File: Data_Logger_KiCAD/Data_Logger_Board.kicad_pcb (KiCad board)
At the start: 6 copper layers, 45 x 63 mm, 107 parts, among them J1 USB_C_Receptacle_USB2.0_16P, J2 Screw_Terminal_01x02, J3 Micro_SD_Card, J4 Conn_Coaxial_Small, J5 Conn_01x02, Q1 Q_NMOS_GSD, SW1 SW_Push, SW2 SW_Push, U1 LSM6DSO32TR, U10 BMP390L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

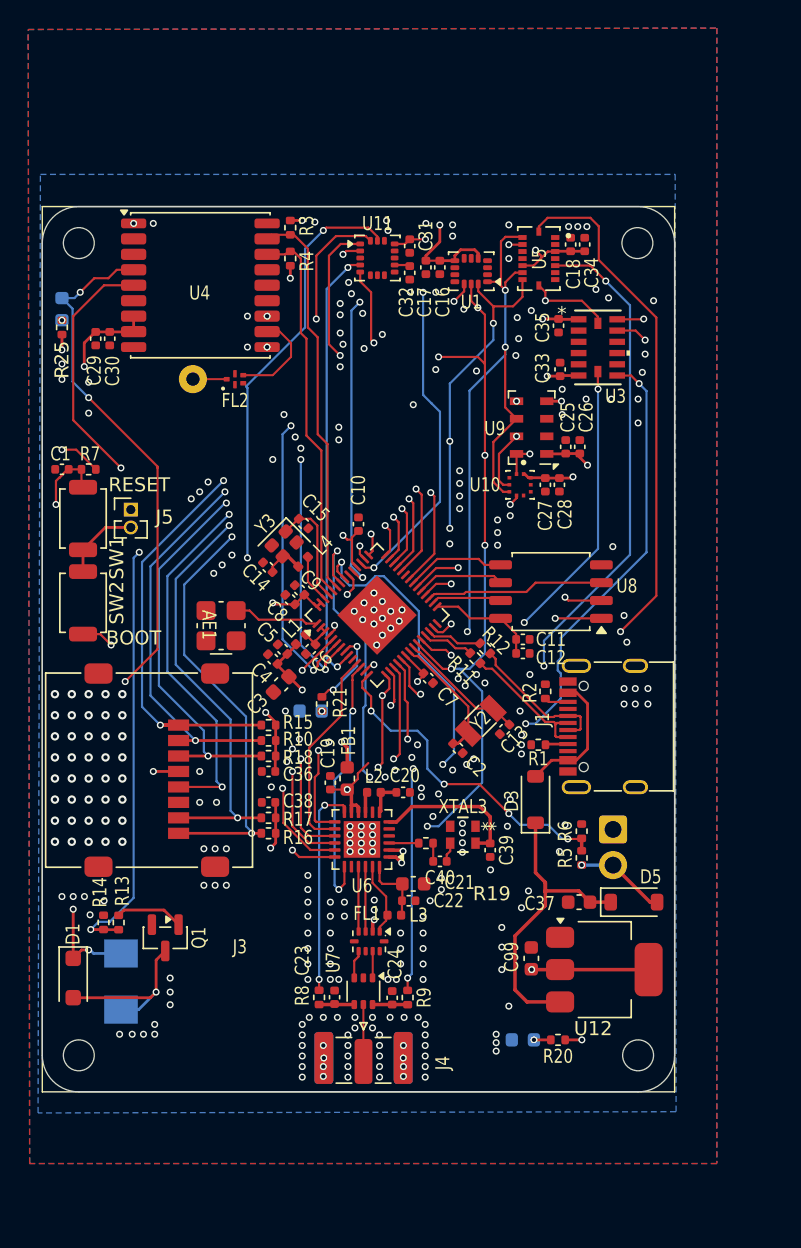
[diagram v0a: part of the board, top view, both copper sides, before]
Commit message: add stitching vias
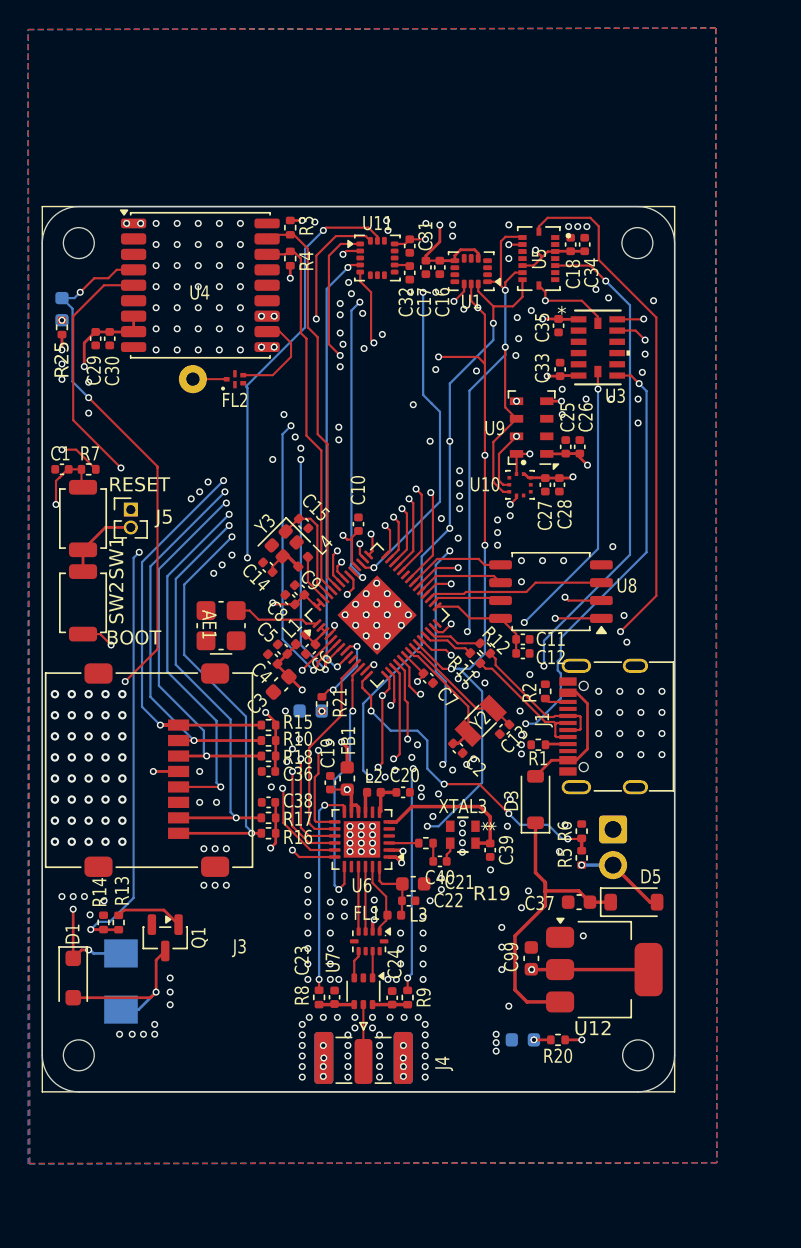
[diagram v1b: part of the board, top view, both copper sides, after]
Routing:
- net /MCU/ANT_SW: track 40.1 -> 43.7 mm, vias 4 -> 5
- net /MCU/MOSI: track 109.8 -> 112.7 mm
- net Net-(U6-VBAT): track 15.5 -> 13.0 mm
- net GND: vias 288 -> 342

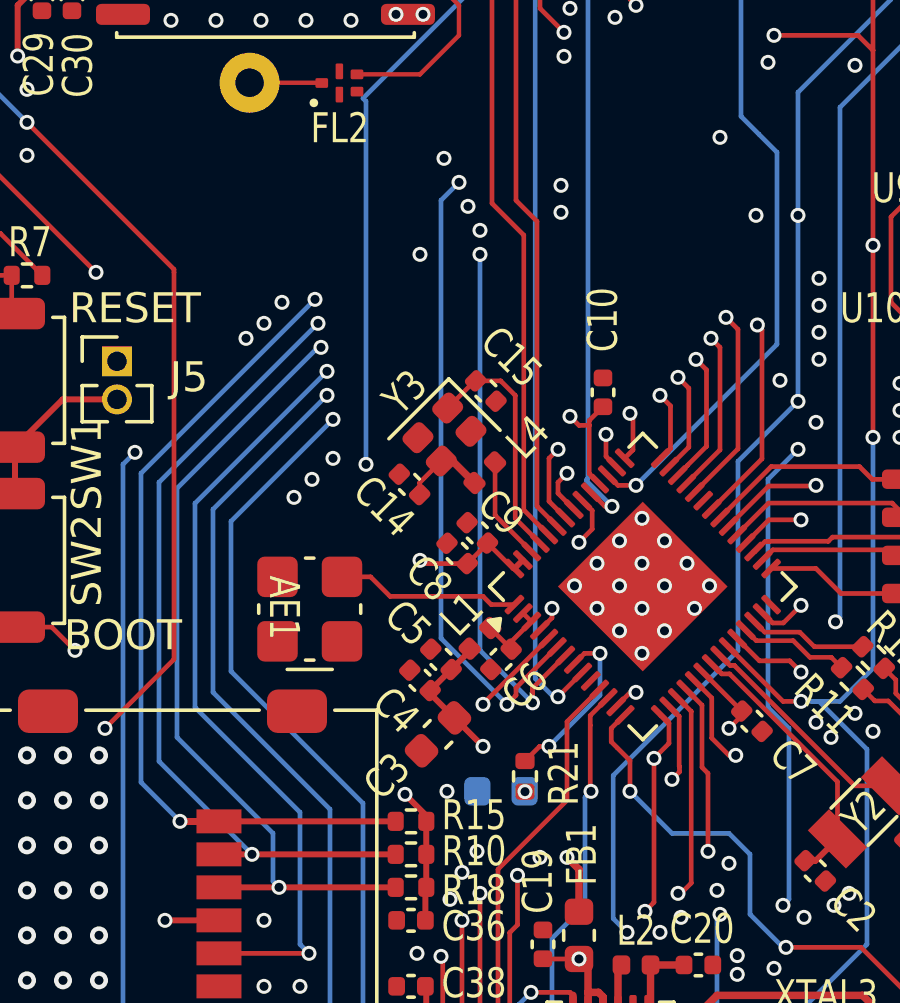
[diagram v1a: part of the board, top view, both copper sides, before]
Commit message: fix missing gnd
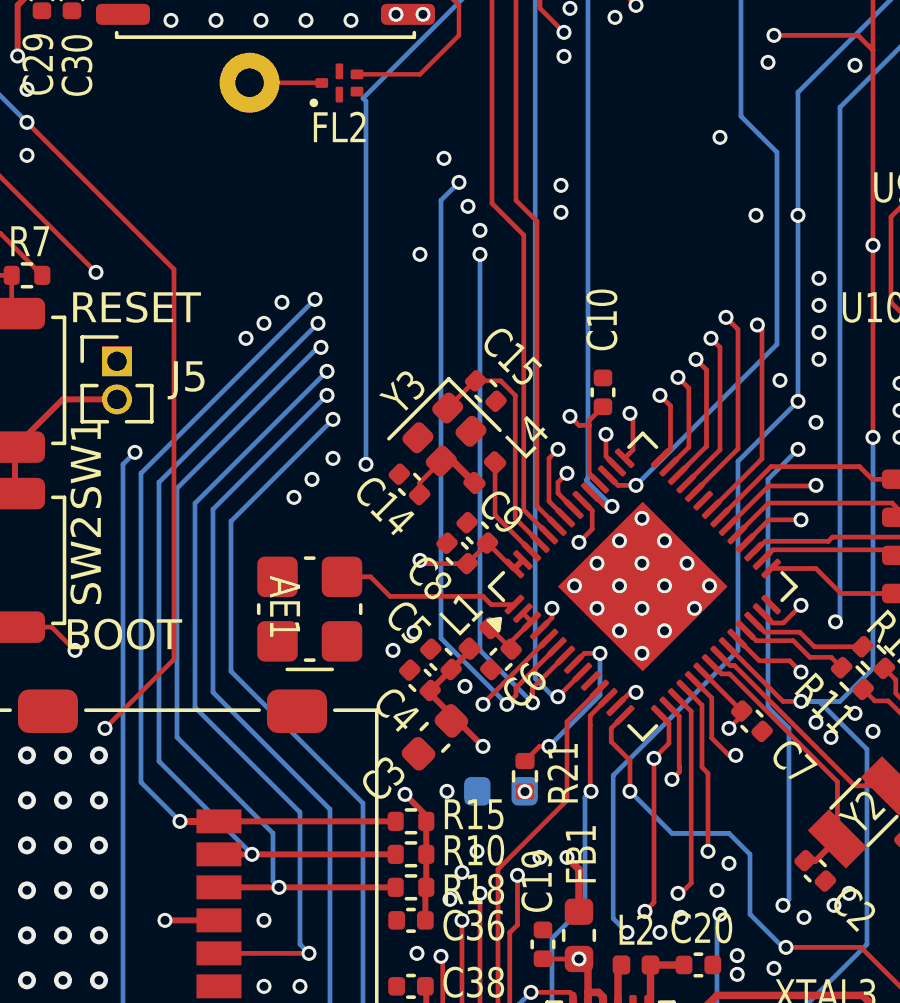
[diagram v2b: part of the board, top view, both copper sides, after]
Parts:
- moved C3 0.14 mm to (136.9, 81.2)
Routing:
- net GND: vias 342 -> 345
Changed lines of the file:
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@@
 	(footprint "Capacitor_SMD:C_0603_1608Metric"
 		(layer "F.Cu")
-		(at 137 81.1 -135)
+		(at 136.9 81.2 -135)
 		(descr "Capacitor SMD 0603 (1608 Metric), square (rectangular) end terminal, IPC-7351 nominal, (Body size source: IPC-SM-782 page 76, https://www.pcb-3d.com/wordpress/wp-content/uploads/ipc-sm-782a_amendment_1_and_2.pdf), generated with kicad-footprint-generator")
 		(tags "capacitor")
@@
 	)
 	(via
+		(at 137.9 79.5)
+		(size 0.5)
+		(drill 0.3)
+		(layers "F.Cu" "B.Cu")
+		(free yes)
+		(net 1)
+	)
+	(via
 		(at 141.75 107.55)
 		(size 0.5)
@@
 	)
 	(via
+		(at 136.2 77.7)
+		(size 0.5)
+		(drill 0.3)
+		(layers "F.Cu" "B.Cu")
+		(free yes)
+		(net 1)
+	)
+	(via
 		(at 138.5 107.55)
 		(size 0.5)
@@
 	)
 	(via
+		(at 135.5 78.3)
+		(size 0.5)
+		(drill 0.3)
+		(layers "F.Cu" "B.Cu")
+		(free yes)
+		(net 1)
+	)
+	(via
 		(at 164.1 84.6)
 		(size 0.5)
@@
 	)
 	(segment
-		(start 121.6 70.9)
-		(end 130.2 79.5)
+		(start 120.975 68.3)
+		(end 121.6 68.925)
 		(width 0.1565)
 		(layer "In2.Cu")
@@
 	)
 	(segment
-		(start 130.2 79.5)
-		(end 138.2 79.5)
+		(start 136.9 79.5)
+		(end 139.5 76.9)
 		(width 0.1565)
 		(layer "In2.Cu")
@@
 	)
 	(segment
-		(start 138.2 79.5)
-		(end 140.8 76.9)
+		(start 121.6 68.925)
+		(end 121.6 70.9)
 		(width 0.1565)
 		(layer "In2.Cu")
@@
 	)
 	(segment
-		(start 121.6 68.925)
-		(end 121.6 70.9)
+		(start 121.6 70.9)
+		(end 130.2 79.5)
 		(width 0.1565)
 		(layer "In2.Cu")
@@
 	)
 	(segment
-		(start 120.975 68.3)
-		(end 121.6 68.925)
+		(start 130.2 79.5)
+		(end 136.9 79.5)
+		(width 0.1565)
+		(layer "In2.Cu")
+		(net 3)
+	)
+	(segment
+		(start 139.5 76.9)
+		(end 140.8 76.9)
 		(width 0.1565)
 		(layer "In2.Cu")
@@
 	)
 	(segment
-		(start 155.9 60.95)
-		(end 156.95 60.95)
-		(width 0.2)
+		(start 139.3 80.1)
+		(end 139.6 79.8)
+		(width 0.1565)
 		(layer "F.Cu")
 		(net 62)
 	)
 	(segment
-		(start 139.6 79.8)
-		(end 139.3 80.1)
-		(width 0.1565)
+		(start 155.9 60.95)
+		(end 156.95 60.95)
+		(width 0.2)
 		(layer "F.Cu")
 		(net 62)
 	)
 	(segment
-		(start 140.961218 78.188349)
-		(end 139.6 79.549567)
+		(start 139.6 79.549567)
+		(end 140.961218 78.188349)
 		(width 0.1565)
 		(layer "F.Cu")
@@
 	)
 	(segment
-		(start 139.6 79.549567)
-		(end 139.6 79.8)
+		(start 139.6 79.8)
+		(end 139.6 79.549567)
 		(width 0.1565)
 		(layer "F.Cu")
@@
 	(segment
 		(start 137.1 77.9)
-		(end 139.3 80.1)
+		(end 137.1 63.3)
 		(width 0.1565)
 		(layer "B.Cu")
@@
 	)
 	(segment
-		(start 137.7 62.7)
-		(end 137.1 63.3)
+		(start 137.1 63.3)
+		(end 137.7 62.7)
 		(width 0.1565)
 		(layer "B.Cu")
@@
 	)
 	(segment
-		(start 137.1 63.3)
+		(start 139.3 80.1)
 		(end 137.1 77.9)
 		(width 0.1565)
@@
 	)
 	(zone
-		(net 77)
-		(net_name "Net-(AE2-A)")
+		(net 82)
+		(net_name "/MCU/SMA_CONN")
 		(layer "F.Cu")
 		(name "$teardrop_padvia$")
 		(hatch none 0.1)
-		(priority 30000)
+		(priority 30001)
 		(attr
 			(teardrop
@@
 		(polygon
 			(pts
-				(xy 132.700785 59.45415) (xy 132.700785 59.30585) (xy 131.27557 58.54853) (xy 130.719 59.38) (xy 131.27557 60.21147)
+				(xy 142.92415 105.7025) (xy 142.77585 105.7025) (xy 142.298223 106.410723) (xy 142.86 107.9385)
+				(xy 143.421777 106.410723)
 			)
 		)
 	)
 	(zone
-		(net 82)
-		(net_name "/MCU/SMA_CONN")
+		(net 77)
+		(net_name "Net-(AE2-A)")
 		(layer "F.Cu")
 		(name "$teardrop_padvia$")
 		(hatch none 0.1)
-		(priority 30001)
+		(priority 30000)
 		(attr
 			(teardrop
@@
 		(polygon
 			(pts
-				(xy 142.92415 105.7025) (xy 142.77585 105.7025) (xy 142.298223 106.410723) (xy 142.86 107.9385)
-				(xy 143.421777 106.410723)
+				(xy 132.700785 59.45415) (xy 132.700785 59.30585) (xy 131.27557 58.54853) (xy 130.719 59.38) (xy 131.27557 60.21147)
 			)
 		)

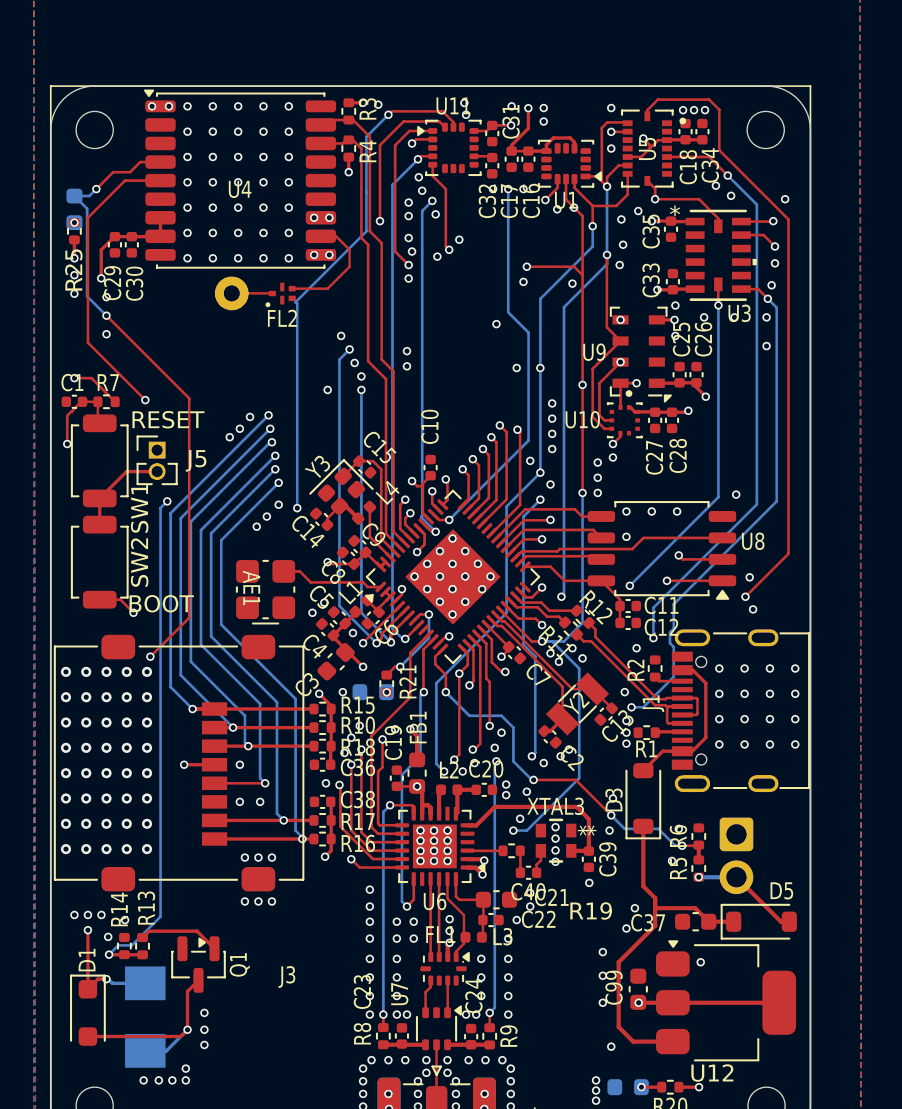
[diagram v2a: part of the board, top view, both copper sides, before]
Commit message: fix gps line
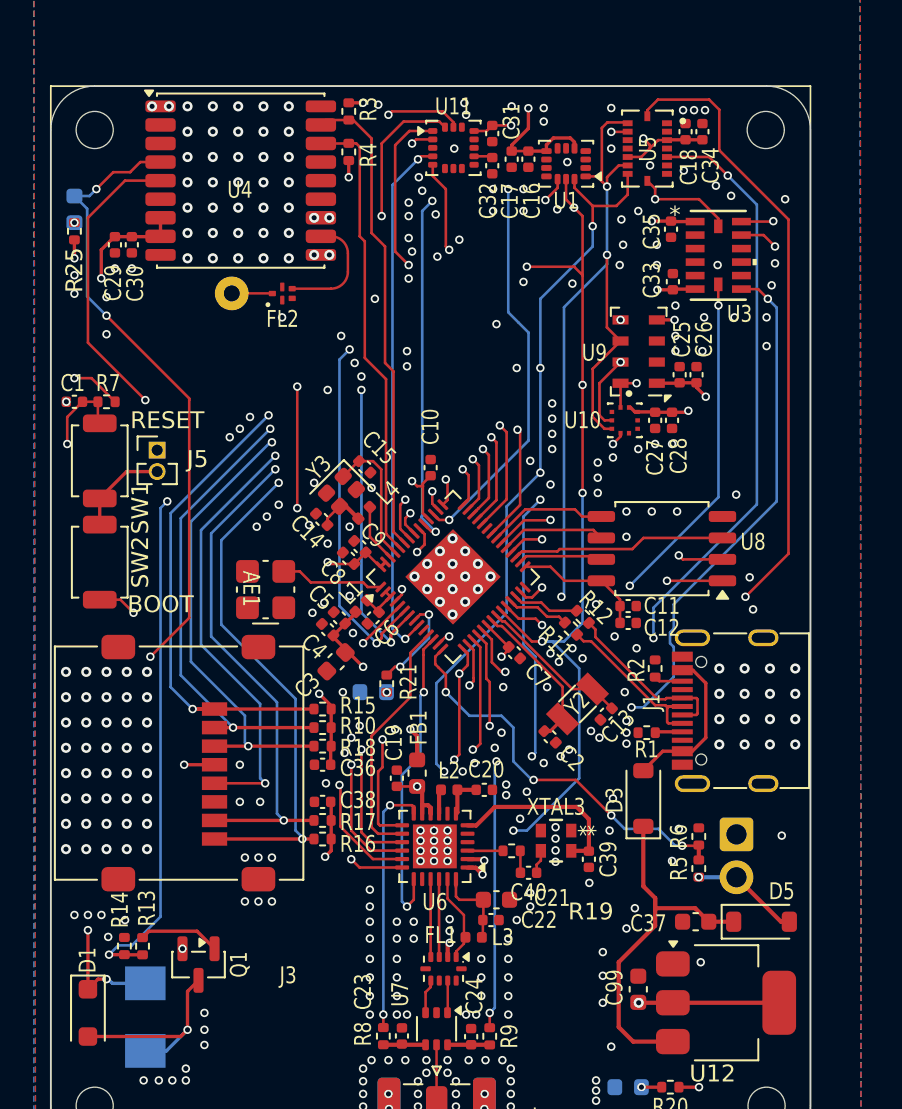
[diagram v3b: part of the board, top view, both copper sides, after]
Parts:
- moved R4 0.20 mm to (137.7, 51.0)
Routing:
- net /MCU/MAG_INT: track 42.3 -> 42.2 mm, vias 3 -> 4
- net GND: vias 345 -> 378

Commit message: review LCSC fields
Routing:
- net GND: vias 378 -> 390
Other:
- board text added: "BATT+"
- board text added: "BATT-"

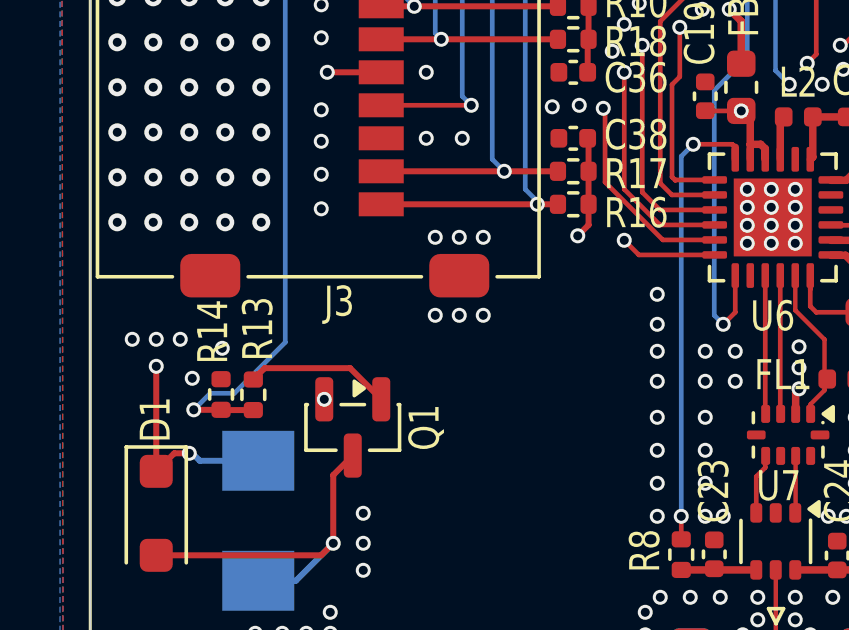
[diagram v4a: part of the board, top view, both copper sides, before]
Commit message: update pcb from schem
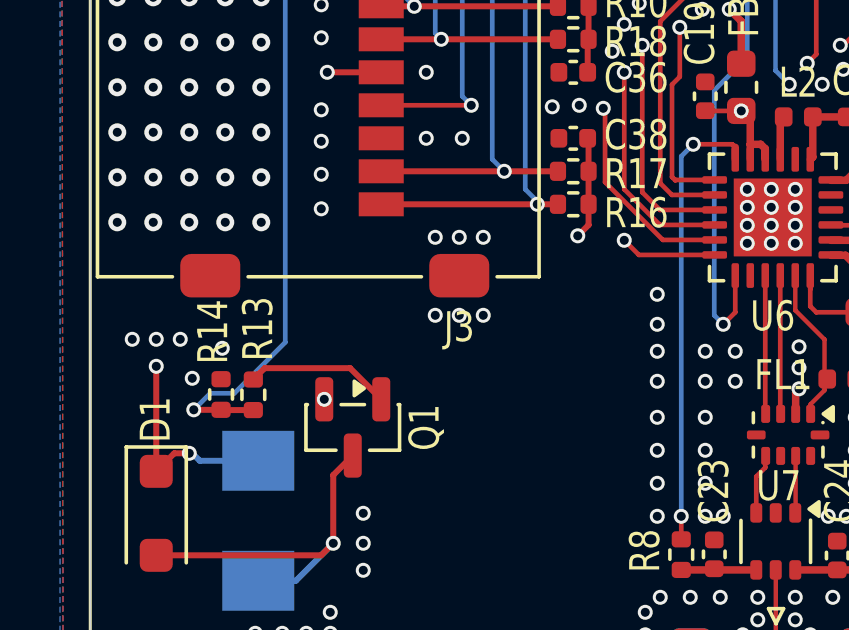
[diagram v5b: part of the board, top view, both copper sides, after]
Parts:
- removed REF**: aiaa-mask-silk-8x4, beavs-footprints:aiaa-mask-silk-8x4
- H1, H2, H3, H4: renamed from REF**; value MountingHole_2.2mm_M2 -> MountingHole
- R20, R21: value 1.5k -> 1k
